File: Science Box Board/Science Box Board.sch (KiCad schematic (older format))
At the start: 40 parts, among them U1 Molex_SL-2, U10 LB1930MC, U11 Molex_SL-10, U12 Molex_SL_2, U13 Molex_SL_5, U2 Molex_SL-2, U3 5V OKI, U4 OPA320, U5 OPA320, U6 5V OKI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

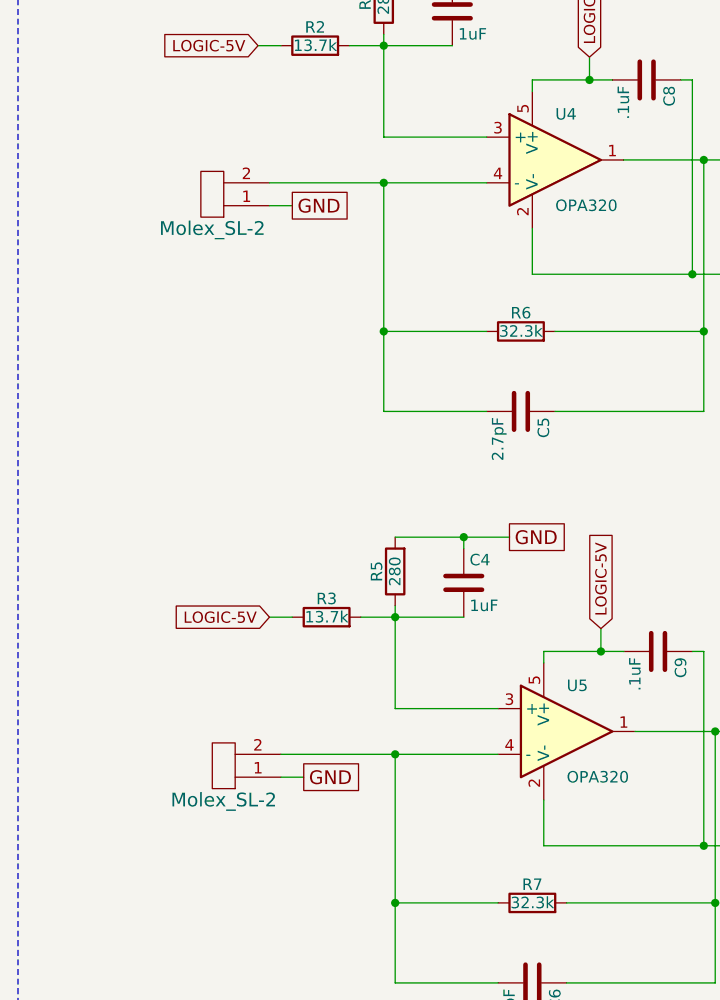
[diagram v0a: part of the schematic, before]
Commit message: Changed Molex SL 2 to SL 3 for photodiodes and added +3v3 to connection
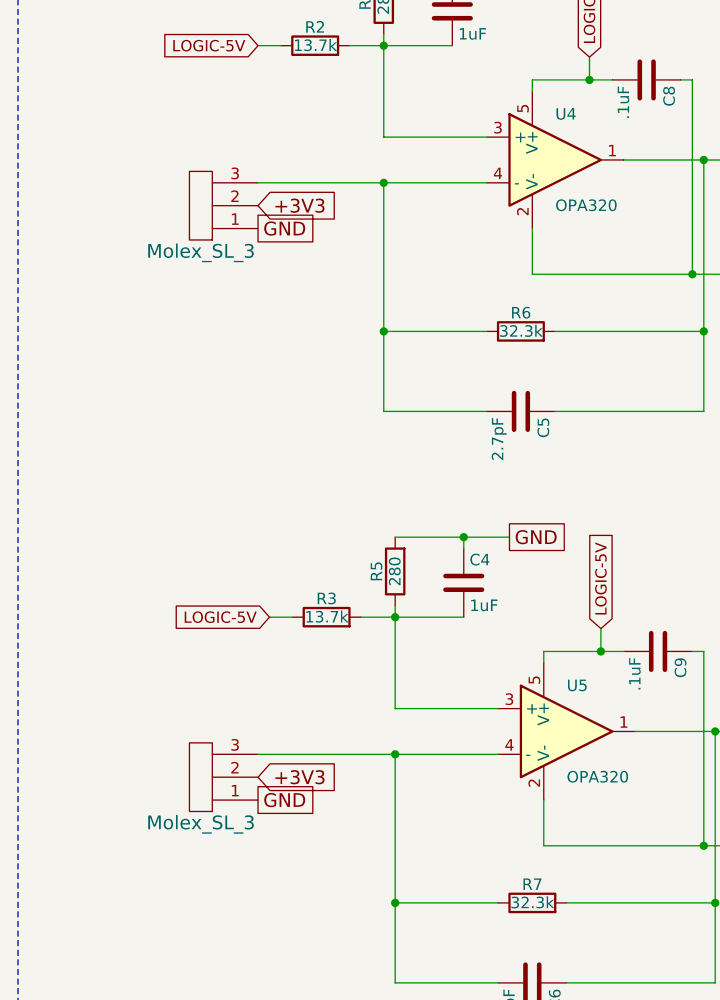
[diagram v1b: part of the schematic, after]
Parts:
- removed U1, U2: Molex_SL-2, MRDT_Connectors:MOLEX_SL_2_Horizontal, symbol Molex_SL_2
- added Conn? (x2): Molex_SL_3, symbol Molex_SL_3
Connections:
- net +3V3: now also Conn?.2, Conn?.2
- net GND: now also Conn?.1, Conn?.1
- net at C5.2, R6.1, U4.4 (-): now also Conn?.3
- net at C6.2, R7.1, U5.4 (-): now also Conn?.3
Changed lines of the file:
@@
 	1    0    0    -1
-$EndComp
-$Comp
-L Molex_SL_2 U1
-U 1 1 5AB1FE22
-P 3400 5150
-F 0 "U1" H 3450 5100 60  0001 C CNN
-F 1 "Molex_SL-2" H 3450 5400 60  0000 C CNN
-F 2 "MRDT_Connectors:MOLEX_SL_2_Horizontal" H 3400 5050 60  0001 C CNN
-F 3 "" H 3400 5050 60  0001 C CNN
-	1    3400 5150
-	-1   0    0    1
 $EndComp
 Text GLabel 3550 4600 0    49   Input ~ 0
@@
 	1    0    0    -1
 $EndComp
-$Comp
-L Molex_SL_2 U2
-U 1 1 5AB21C1D
-P 3450 7650
-F 0 "U2" H 3500 7600 60  0001 C CNN
-F 1 "Molex_SL-2" H 3500 7900 60  0000 C CNN
-F 2 "MRDT_Connectors:MOLEX_SL_2_Horizontal" H 3450 7550 60  0001 C CNN
-F 3 "" H 3450 7550 60  0001 C CNN
-	1    3450 7650
-	-1   0    0    1
-$EndComp
 Text GLabel 3600 7100 0    49   Input ~ 0
 LOGIC-5V
@@
 	2500 4150 7150 4150
 Wire Wire Line
-	3600 5300 3700 5300
-Wire Wire Line
-	3600 5200 4550 5200
+	3550 5200 4550 5200
 Wire Wire Line
 	3550 4600 3650 4600
@@
 Connection ~ 5000 4750
 Wire Wire Line
-	3650 7800 3750 7800
-Wire Wire Line
-	3650 7700 4600 7700
+	3550 7700 4600 7700
 Wire Wire Line
 	3600 7100 3700 7100
@@
 Text GLabel 5700 3100 0    60   UnSpc ~ 0
 GND
-Text GLabel 3700 5300 2    60   UnSpc ~ 0
-GND
-Text GLabel 3750 7800 2    60   UnSpc ~ 0
+Text GLabel 3550 5400 2    60   UnSpc ~ 0
+GND
+Text GLabel 3550 7900 2    60   UnSpc ~ 0
 GND
 Connection ~ 5500 8100
@@
 Text GLabel 9500 5550 2    49   Output ~ 0
 LOGIC-5V
+$Comp
+L Molex_SL_3 Conn?
+U 1 1 5AD93F33
+P 3350 5150
+F 0 "Conn?" H 3400 5100 60  0001 C CNN
+F 1 "Molex_SL_3" H 3400 5500 60  0000 C CNN
+F 2 "" H 3350 5150 60  0001 C CNN
+F 3 "" H 3350 5150 60  0001 C CNN
+	1    3350 5150
+	-1   0    0    1
+$EndComp
+Text GLabel 3550 5300 2    60   Input ~ 0
++3V3
+$Comp
+L Molex_SL_3 Conn?
+U 1 1 5AD94E13
+P 3350 7650
+F 0 "Conn?" H 3400 7600 60  0001 C CNN
+F 1 "Molex_SL_3" H 3400 8000 60  0000 C CNN
+F 2 "" H 3350 7650 60  0001 C CNN
+F 3 "" H 3350 7650 60  0001 C CNN
+	1    3350 7650
+	-1   0    0    1
+$EndComp
+Text GLabel 3550 7800 2    60   Input ~ 0
++3V3
 $EndSCHEMATC
